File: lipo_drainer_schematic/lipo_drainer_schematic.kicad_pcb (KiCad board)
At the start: 2 copper layers, 122 x 88 mm, 62 parts, among them J1 BATT, J2 FAN, J3 Vcal, J4 128x64_OLED, J5 Gcal, J6 ICAL, J7 MCP7901, Q1 MMBT3904, Q10 G700P06T, Q11 G700P06T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

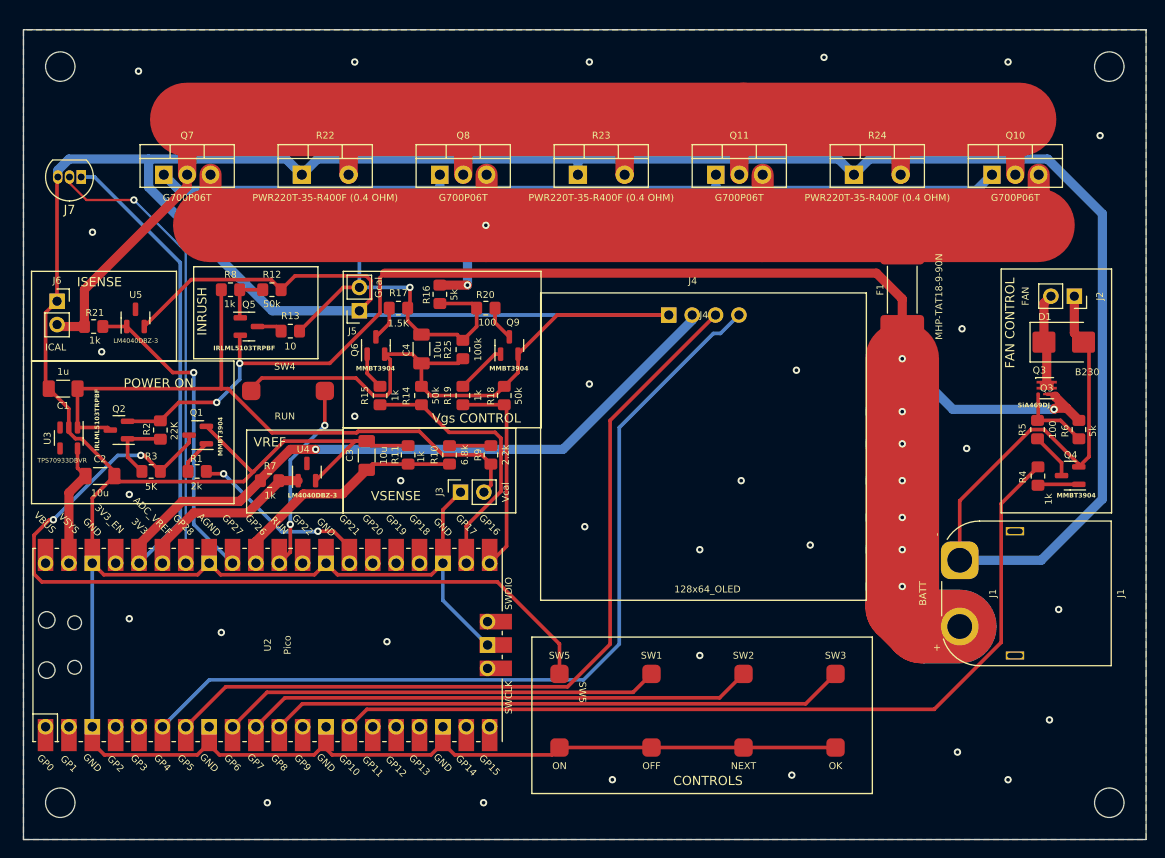
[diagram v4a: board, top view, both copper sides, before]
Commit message: Changed OFF button to be directly connected to the FET
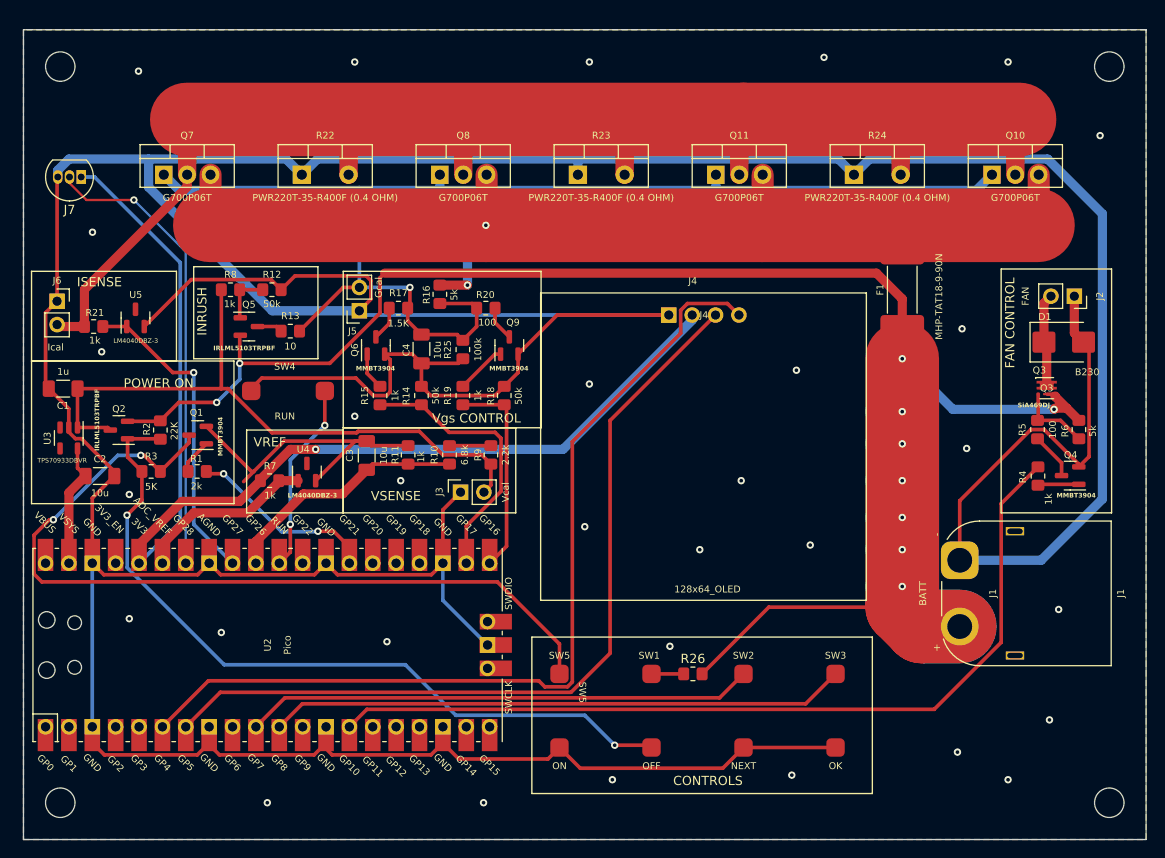
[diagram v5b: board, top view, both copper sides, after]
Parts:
- added R26: 100, Resistor_SMD:R_0805_2012Metric_Pad1.20x1.40mm_HandSolder, F.Cu at (160.8, 120.0)
- J6: value ICAL -> Ical
- moved SW1 8.00 mm to (156.2, 128.0), turned to 0 degrees
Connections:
- Q2 pad 1: Net-(Q2-G) -> /OFF
- R2 pad 2: Net-(Q2-G) -> /OFF
- R3 pad 1: Net-(Q2-G) -> /OFF
- SW1 pad 2: GND -> Net-(R26-Pad1)
- U2 pad 9: /OFF -> unconnected-(U2-GPIO6-Pad9)
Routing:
- net /OFF: track 47.9 -> 84.0 mm, vias 0 -> 2
- net /BAT+: track 191.3 -> 216.1 mm
- net GND: track 647.1 -> 635.0 mm
- net Net-(Q2-G): track 7.78 -> 0.00 mm
- net /SDA: track 95.0 -> 99.5 mm
- net Net-(R26-Pad1): track 0.00 -> 3.50 mm
- net /SCL: track 90.3 -> 90.9 mm
